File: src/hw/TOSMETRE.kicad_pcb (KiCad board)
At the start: 2 copper layers, 177.8 x 101.6 mm, 15 parts, among them J1 +, J2 -, J3 Conn_01x01, J4 Conn_01x01, U1 16F88_SSOP, U2 L7805, Y1 Crystal

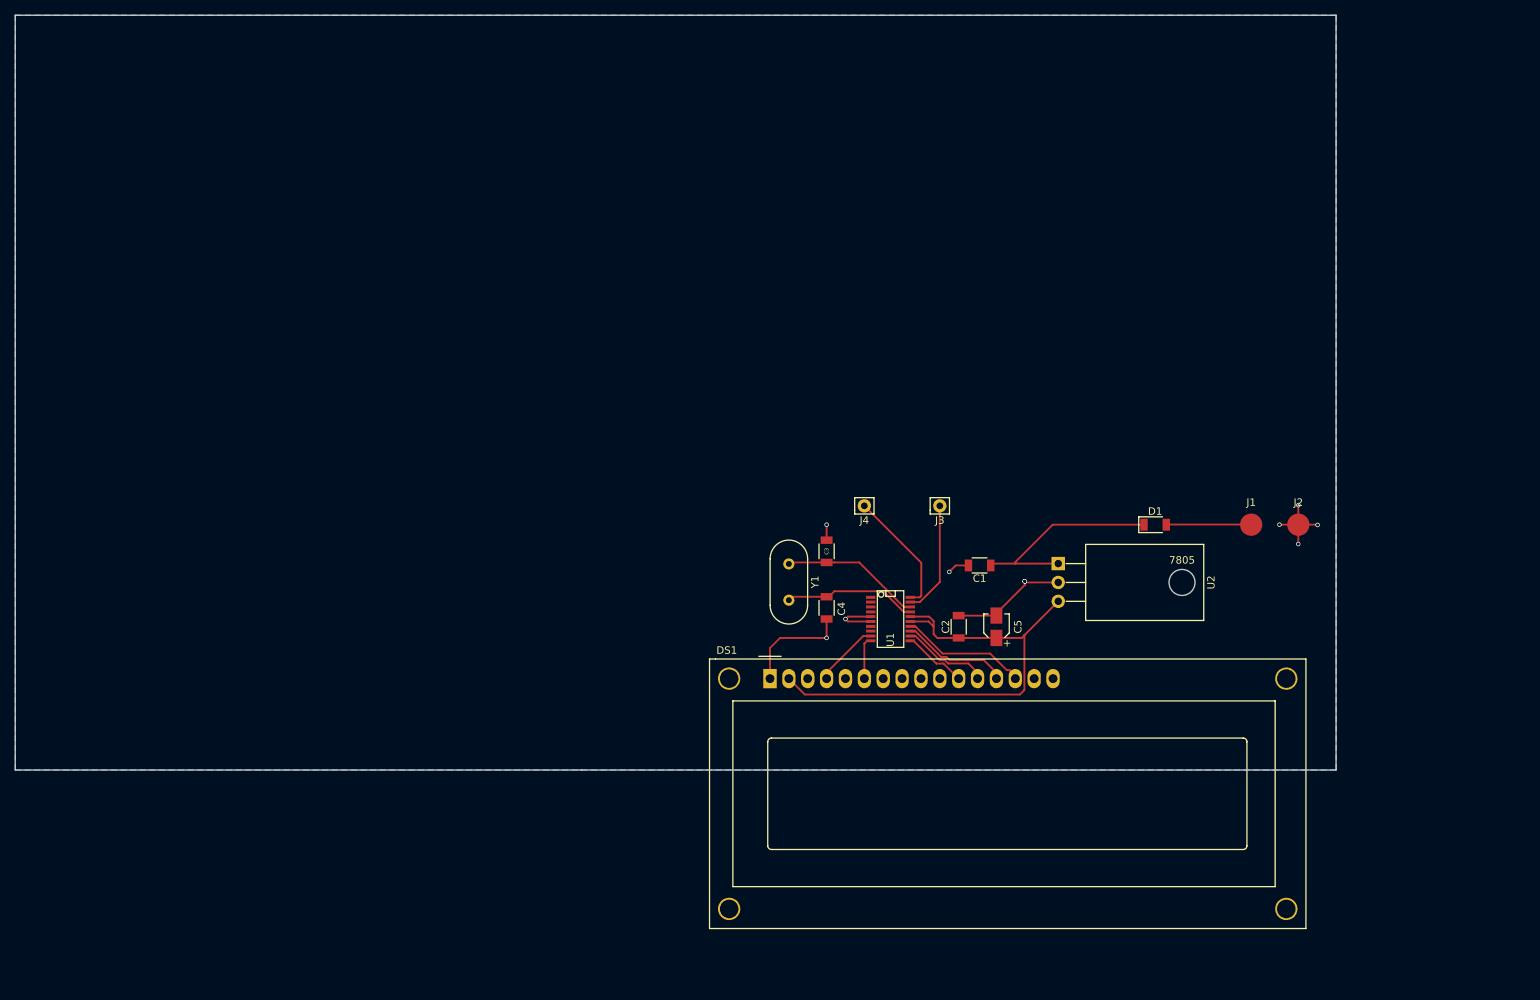
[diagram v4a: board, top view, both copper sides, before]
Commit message: preparation pour mise a la taille du PCB pour Boitier Disponible au RC
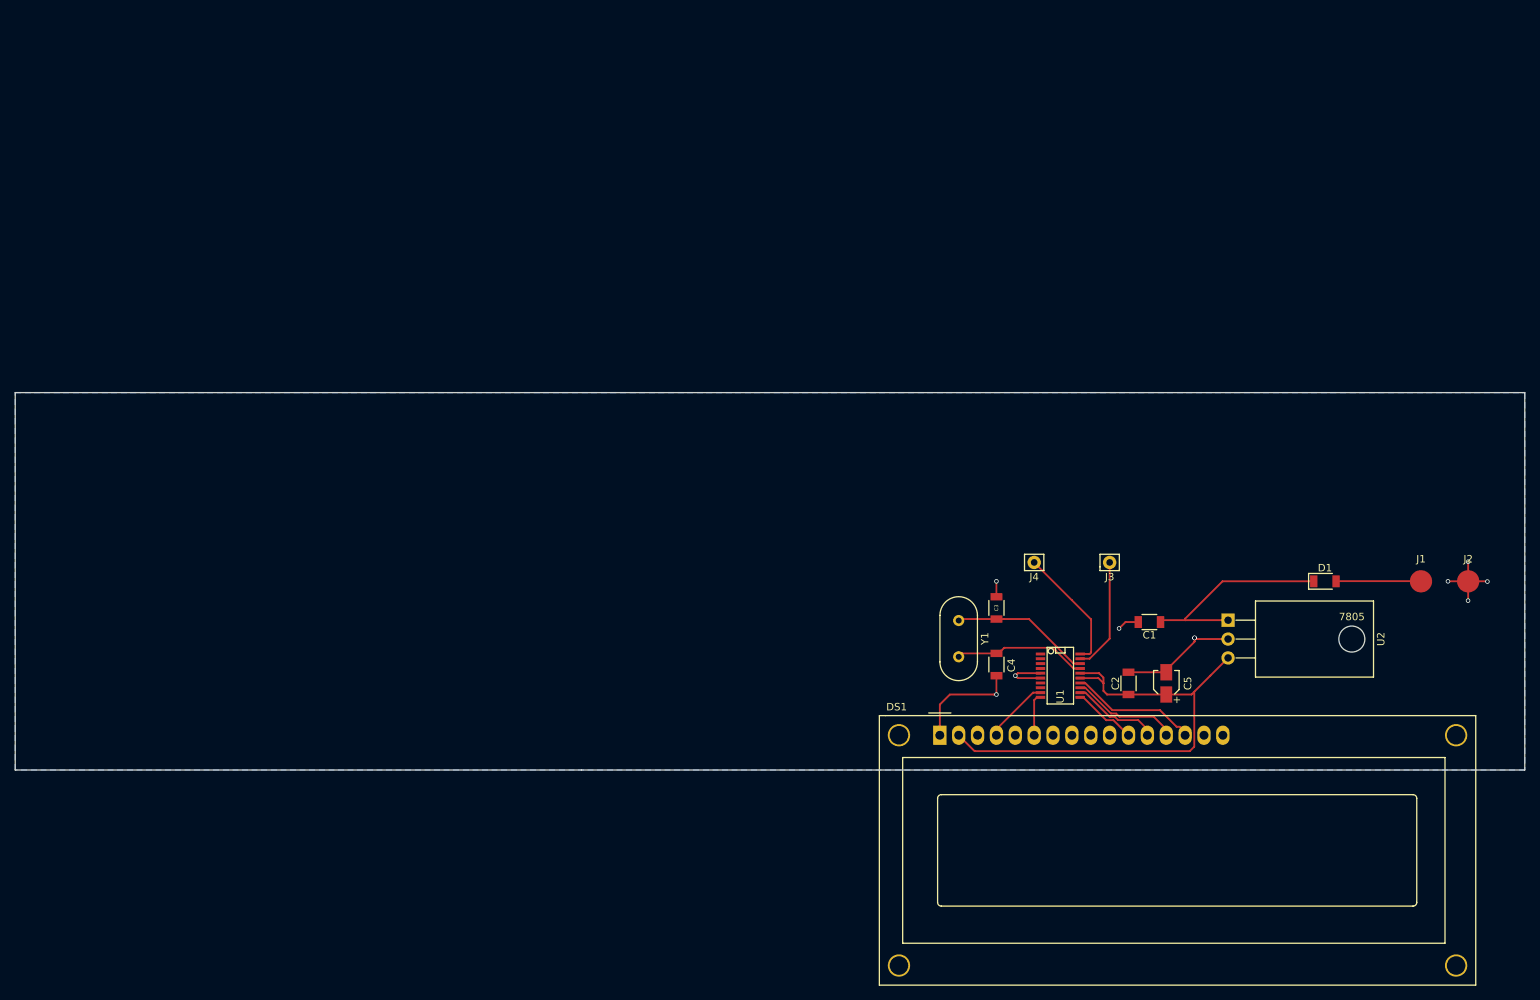
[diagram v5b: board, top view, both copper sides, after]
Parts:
- moved 7805 24.1 mm to (238.3, 137.3)
- moved C1 24.1 mm to (211.1, 135.0)
- moved C2 24.1 mm to (208.3, 143.3)
- moved C3 24.1 mm to (190.5, 133.1)
- moved C4 24.1 mm to (190.5, 140.7)
- moved C5 24.1 mm to (213.4, 143.3)
- moved J3 24.1 mm to (205.7, 127.0)
- moved J4 24.1 mm to (195.6, 127.0)
- moved U1 24.1 mm to (199.1, 142.2)
- moved J1 24.1 mm to (247.7, 129.5)
- moved J2 24.1 mm to (254.0, 129.5)
- moved DS1 24.1 mm to (182.9, 150.3)
- moved U2 24.1 mm to (221.7, 134.8)
- moved D1 24.1 mm to (234.7, 129.5)
- moved Y1 24.1 mm to (185.4, 134.8)
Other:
- board size 177.8 x 101.6 mm -> 203.2 x 50.8 mm

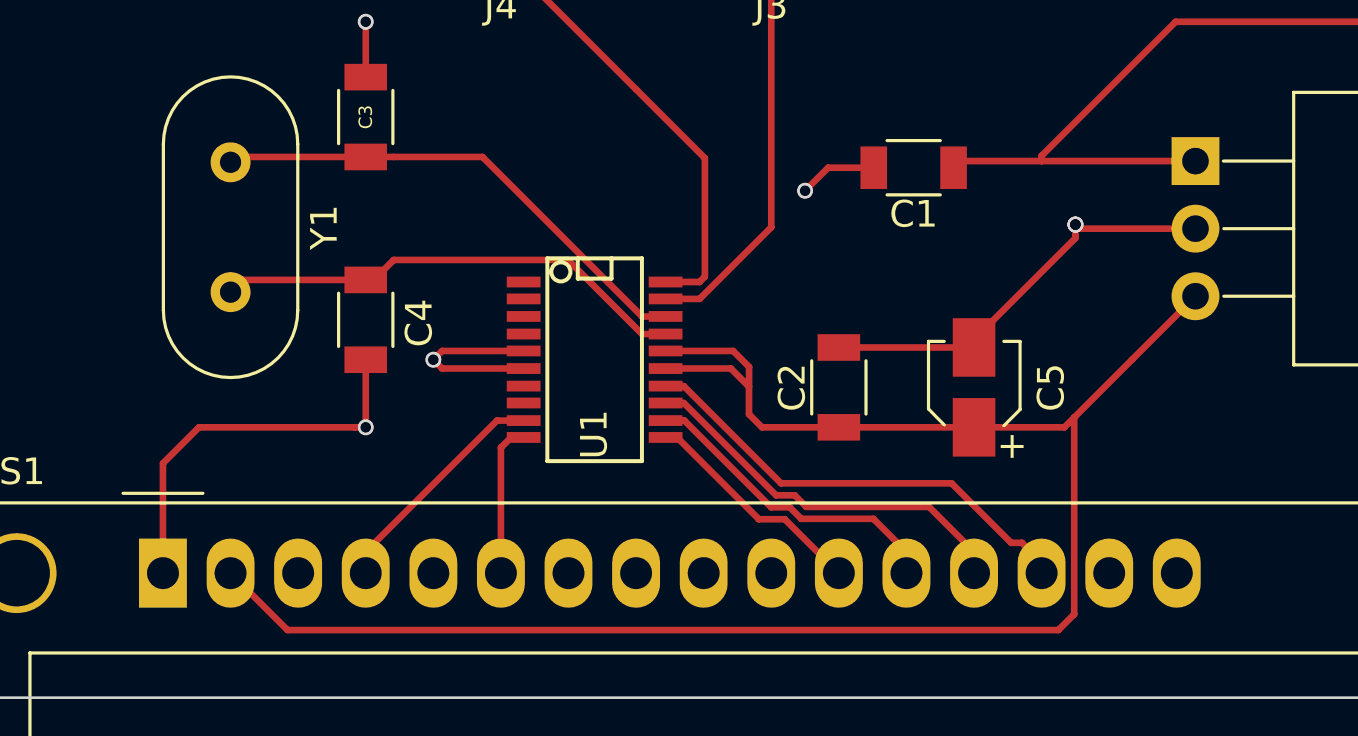
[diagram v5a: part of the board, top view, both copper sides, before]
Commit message: Modif piste pour "esthetique"
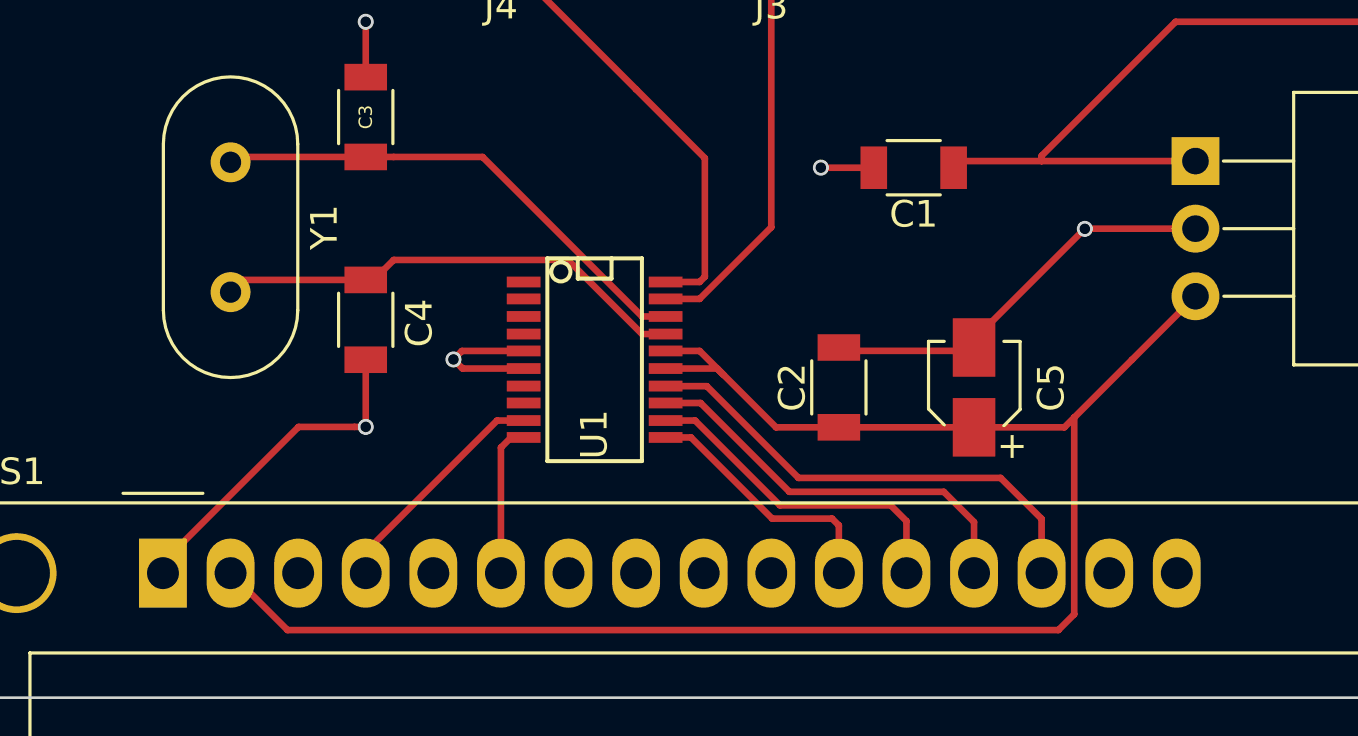
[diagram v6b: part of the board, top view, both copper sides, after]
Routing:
- net GNDREF: track 53.4 -> 48.0 mm, vias 10 -> 9
- net Net-(C2-Pad1): track 68.2 -> 66.1 mm
- net Net-(DS1-Pad14): track 16.9 -> 17.8 mm
- net Net-(DS1-Pad11): track 8.46 -> 9.27 mm
- net Net-(DS1-Pad12): track 11.5 -> 12.2 mm
- net Net-(DS1-Pad13): track 14.3 -> 15.0 mm

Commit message: MODIF OPTIMISATION EN COURS AVEC SUPPRESSION Q ET CAPA
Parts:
- moved C2 5.93 mm to (211.9, 138.6)
- moved C5 5.08 mm to (215.5, 138.7)
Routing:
- net (no net): track 0.00 -> 230.3 mm
- net Net-(DS1-Pad14): track 17.8 -> 23.3 mm
- net GNDREF: track 48.0 -> 43.0 mm
- net Net-(DS1-Pad13): track 15.0 -> 19.5 mm
- net Net-(DS1-Pad6): track 5.33 -> 8.22 mm
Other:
- board text added: "PGM"
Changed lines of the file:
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@@
   (general
     (links 29)
-    (no_connects 0)
+    (no_connects 1)
     (area 55.92 104.089999 261.670001 185.995)
     (thickness 1.6)
-    (drawings 9)
-    (tracks 110)
+    (drawings 10)
+    (tracks 130)
     (zones 0)
     (modules 15)
@@
     (0 F.Cu signal)
     (31 B.Cu signal)
-    (32 B.Adhes user hide)
-    (33 F.Adhes user hide)
-    (34 B.Paste user hide)
-    (35 F.Paste user hide)
+    (32 B.Adhes user)
+    (33 F.Adhes user)
+    (34 B.Paste user)
+    (35 F.Paste user)
     (36 B.SilkS user hide)
     (37 F.SilkS user hide)
@@
     (39 F.Mask user hide)
     (40 Dwgs.User user hide)
-    (41 Cmts.User user)
-    (42 Eco1.User user)
+    (41 Cmts.User user hide)
+    (42 Eco1.User user hide)
     (43 Eco2.User user hide)
     (44 Edge.Cuts user hide)
-    (45 Margin user)
-    (46 B.CrtYd user)
+    (45 Margin user hide)
+    (46 B.CrtYd user hide)
     (47 F.CrtYd user hide)
     (48 B.Fab user hide)
@@
   )
   (module Capacitors_SMD:C_1206 (layer F.Cu)
-    (at 208.28 143.28 90)
+    (at 211.9376 138.6092 90)
     (descr "Capacitor SMD 1206, reflow soldering, AVX (see smccp.pdf)")
     (tags "capacitor 1206")
@@
   )
   (module Capacitors_SMD:CP_Elec_3x5.3 (layer F.Cu)
-    (at 213.36 143.28 90)
+    (at 215.4682 138.6572 90)
     (descr "SMT capacitor, aluminium electrolytic, 3x5.3")
     (attr smd)
@@
       (net 6 "Net-(D1-Pad2)"))
   )
+  (gr_text PGM (at 197.231 147.5994) (layer F.Cu)
+    (effects (font (size 0.2 0.2) (thickness 0.05)))
+  )
   (target plus (at 58.42 154.94) (size 5) (width 0.1) (layer Edge.Cuts))
   (target plus (at 58.42 154.94) (size 5) (width 0.1) (layer Edge.Cuts))
@@
   (gr_line (start 261.62 154.94) (end 261.62 104.14) (layer Edge.Cuts) (width 0.1))
   (gr_line (start 134.62 154.94) (end 261.62 154.94) (layer Edge.Cuts) (width 0.1))
+  (segment (start 131.1148 125.2728) (end 186.5122 125.2728) (width 0.25) (layer F.Cu) (net 0))
+  (segment (start 130.302 124.46) (end 131.1148 125.2728) (width 0.25) (layer F.Cu) (net 0))
+  (segment (start 131.9276 124.46) (end 130.302 124.46) (width 0.25) (layer F.Cu) (net 0))
+  (segment (start 124.4092 111.3028) (end 203.454 111.3028) (width 0.25) (layer F.Cu) (net 0))
+  (segment (start 118.2116 116.6622) (end 211.2518 116.6622) (width 0.25) (layer F.Cu) (net 0))
   (segment (start 233.22 129.54) (end 220.93612 129.54) (width 0.25) (layer F.Cu) (net 1))
   (segment (start 220.93612 129.54) (end 215.9 134.57612) (width 0.25) (layer F.Cu) (net 1))
@@
   (segment (start 212.592 134.724) (end 212.592 135.024) (width 0.25) (layer F.Cu) (net 1))
   (segment (start 212.592 135.324) (end 212.592 135.024) (width 0.25) (layer F.Cu) (net 1))
+  (segment (start 209.592 135.024) (end 209.592 136.074) (width 0.25) (layer F.Cu) (net 2))
+  (segment (start 210.8876 137.1092) (end 211.9376 137.1092) (width 0.25) (layer F.Cu) (net 2))
+  (segment (start 209.592 136.074) (end 210.6272 137.1092) (width 0.25) (layer F.Cu) (net 2))
+  (segment (start 210.6272 137.1092) (end 210.8876 137.1092) (width 0.25) (layer F.Cu) (net 2))
+  (segment (start 215.448768 137.321882) (end 217.524099 137.321882) (width 0.25) (layer F.Cu) (net 2))
   (segment (start 190.5 144.76485) (end 190.499837 144.765013) (width 0.25) (layer F.Cu) (net 2))
   (segment (start 190.075573 144.765013) (end 190.499837 144.765013) (width 0.25) (layer F.Cu) (net 2))
@@
   (segment (start 209.592 135.024) (end 207.607269 135.024) (width 0.25) (layer F.Cu) (net 2))
   (via (at 207.60435 135.021081) (size 0.6) (drill 0.4) (layers F.Cu B.Cu) (net 2))
-  (segment (start 217.518118 137.321882) (end 217.524099 137.321882) (width 0.25) (layer F.Cu) (net 2))
-  (segment (start 213.36 141.48) (end 217.518118 137.321882) (width 0.25) (layer F.Cu) (net 2))
   (segment (start 217.531981 137.314) (end 217.524099 137.321882) (width 0.25) (layer F.Cu) (net 2))
   (segment (start 221.682 137.314) (end 217.531981 137.314) (width 0.25) (layer F.Cu) (net 2))
@@
   (via (at 190.5 129.54) (size 0.6) (drill 0.4) (layers F.Cu B.Cu) (net 2))
   (segment (start 190.5 131.62) (end 190.5 129.54) (width 0.25) (layer F.Cu) (net 2))
-  (segment (start 208.28 141.907) (end 213.36 141.907) (width 0.25) (layer F.Cu) (net 2))
   (via (at 253.986599 132.142827) (size 0.6) (drill 0.4) (layers F.Cu B.Cu) (net 2))
   (via (at 256.59007 129.572312) (size 0.6) (drill 0.4) (layers F.Cu B.Cu) (net 2))
@@
   (segment (start 254 129.54) (end 256.54 129.54) (width 0.25) (layer F.Cu) (net 2))
   (segment (start 209.592 135.024) (end 209.592 135.324) (width 0.25) (layer F.Cu) (net 2))
-  (segment (start 203.95239 142.813321) (end 203.048869 141.9098) (width 0.25) (layer F.Cu) (net 3))
-  (segment (start 203.048869 141.9098) (end 201.769 141.9098) (width 0.25) (layer F.Cu) (net 3))
-  (segment (start 201.769 142.5702) (end 203.709268 142.5702) (width 0.25) (layer F.Cu) (net 3))
-  (segment (start 203.709268 142.5702) (end 205.919068 144.78) (width 0.25) (layer F.Cu) (net 3))
-  (segment (start 205.919068 144.78) (end 208.28 144.78) (width 0.25) (layer F.Cu) (net 3))
+  (segment (start 211.9376 140.1092) (end 215.4202 140.1092) (width 0.25) (layer F.Cu) (net 3))
+  (segment (start 215.4202 140.1092) (end 215.4682 140.1572) (width 0.25) (layer F.Cu) (net 3))
+  (segment (start 217.146055 139.860961) (end 217.142413 139.864603) (width 0.25) (layer F.Cu) (net 3))
+  (segment (start 217.142413 139.864603) (end 217.142413 142.659882) (width 0.25) (layer F.Cu) (net 3))
+  (segment (start 201.769 142.5702) (end 207.8482 142.5702) (width 0.25) (layer F.Cu) (net 3))
+  (segment (start 207.8482 142.5702) (end 210.3092 140.1092) (width 0.25) (layer F.Cu) (net 3))
+  (segment (start 210.3092 140.1092) (end 211.9376 140.1092) (width 0.25) (layer F.Cu) (net 3))
+  (segment (start 212.117916 140.235936) (end 212.155105 140.273125) (width 0.25) (layer F.Cu) (net 3))
   (segment (start 185.42 150.26) (end 187.56 152.4) (width 0.25) (layer F.Cu) (net 3))
   (segment (start 187.56 152.4) (end 216.530493 152.4) (width 0.25) (layer F.Cu) (net 3))
   (segment (start 216.530493 152.4) (end 217.12501 151.805483) (width 0.25) (layer F.Cu) (net 3))
-  (segment (start 217.12501 151.805483) (end 217.12501 144.41099) (width 0.25) (layer F.Cu) (net 3))
-  (segment (start 213.36 144.78) (end 216.756 144.78) (width 0.25) (layer F.Cu) (net 3))
-  (segment (start 216.756 144.78) (end 217.12501 144.41099) (width 0.25) (layer F.Cu) (net 3))
-  (segment (start 213.36 144.78) (end 208.28 144.78) (width 0.25) (layer F.Cu) (net 3))
+  (segment (start 217.12501 151.805483) (end 217.12501 142.676086) (width 0.25) (layer F.Cu) (net 3))
+  (segment (start 215.857203 139.854) (end 221.682 139.854) (width 0.25) (layer F.Cu) (net 3))
+  (segment (start 201.878061 142.583622) (end 201.806439 142.512) (width 0.25) (layer F.Cu) (net 3))
+  (segment (start 201.806439 142.512) (end 201.806439 141.909021) (width 0.25) (layer F.Cu) (net 3))
+  (segment (start 201.806439 141.909021) (end 201.80566 141.9098) (width 0.25) (layer F.Cu) (net 3))
+  (segment (start 201.80566 141.9098) (end 201.769 141.9098) (width 0.25) (layer F.Cu) (net 3))
   (segment (start 185.42 149.86) (end 185.42 150.26) (width 0.25) (layer F.Cu) (net 3))
-  (segment (start 217.12501 144.41099) (end 219.296 142.24) (width 0.25) (layer F.Cu) (net 3))
-  (segment (start 219.296 142.24) (end 221.682 139.854) (width 0.25) (layer F.Cu) (net 3))
   (segment (start 190.5 134.62) (end 185.62 134.62) (width 0.25) (layer F.Cu) (net 4))
   (segment (start 185.62 134.62) (end 185.42 134.82) (width 0.25) (layer F.Cu) (net 4))
@@
   (segment (start 195.434 144.526) (end 190.5 149.46) (width 0.25) (layer F.Cu) (net 7))
   (segment (start 190.5 149.46) (end 190.5 149.86) (width 0.25) (layer F.Cu) (net 7))
+  (segment (start 197.993 145.834) (end 197.993 146.8882) (width 0.25) (layer F.Cu) (net 8))
+  (segment (start 196.435 145.161) (end 197.32 145.161) (width 0.25) (layer F.Cu) (net 8))
+  (segment (start 197.32 145.161) (end 197.993 145.834) (width 0.25) (layer F.Cu) (net 8))
   (segment (start 195.961 145.161) (end 195.58 145.542) (width 0.25) (layer F.Cu) (net 8))
   (segment (start 195.58 145.542) (end 195.58 149.86) (width 0.25) (layer F.Cu) (net 8))
@@
   (segment (start 210.227953 147.712356) (end 210.82 148.304403) (width 0.25) (layer F.Cu) (net 10))
   (segment (start 210.82 148.304403) (end 210.82 149.86) (width 0.25) (layer F.Cu) (net 10))
+  (segment (start 198.9074 145.964398) (end 198.9074 146.812) (width 0.25) (layer F.Cu) (net 11))
+  (segment (start 201.769 143.8656) (end 201.006198 143.8656) (width 0.25) (layer F.Cu) (net 11))
+  (segment (start 201.006198 143.8656) (end 198.9074 145.964398) (width 0.25) (layer F.Cu) (net 11))
   (segment (start 201.769 143.8656) (end 203.082688 143.8656) (width 0.25) (layer F.Cu) (net 11))
   (segment (start 203.082688 143.8656) (end 206.421344 147.204256) (width 0.25) (layer F.Cu) (net 11))
@@
   (segment (start 212.22523 147.204256) (end 213.36 148.339026) (width 0.25) (layer F.Cu) (net 11))
   (segment (start 213.36 148.339026) (end 213.36 149.86) (width 0.25) (layer F.Cu) (net 11))
+  (segment (start 198.4502 145.6644) (end 198.4502 146.8374) (width 0.25) (layer F.Cu) (net 12))
+  (segment (start 198.4502 146.8374) (end 198.44301 146.84459) (width 0.25) (layer F.Cu) (net 12))
+  (segment (start 201.769 143.2306) (end 200.884 143.2306) (width 0.25) (layer F.Cu) (net 12))
+  (segment (start 200.884 143.2306) (end 198.4502 145.6644) (width 0.25) (layer F.Cu) (net 12))
   (segment (start 203.315106 143.233437) (end 206.763193 146.681524) (width 0.25) (layer F.Cu) (net 12))
   (segment (start 202.287512 143.2306) (end 202.290349 143.233437) (width 0.25) (layer F.Cu) (net 12))
